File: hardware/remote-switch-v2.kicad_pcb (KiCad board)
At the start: 2 copper layers, 40 x 25 mm, 27 parts, among them J1 Debug, P1 CON-SENSOR2, P2 BOOT, U1 XMC1302-32, U2 RFM69HW, U3 DRILL, U4 DRILL, U5 DRILL, U6 DRILL

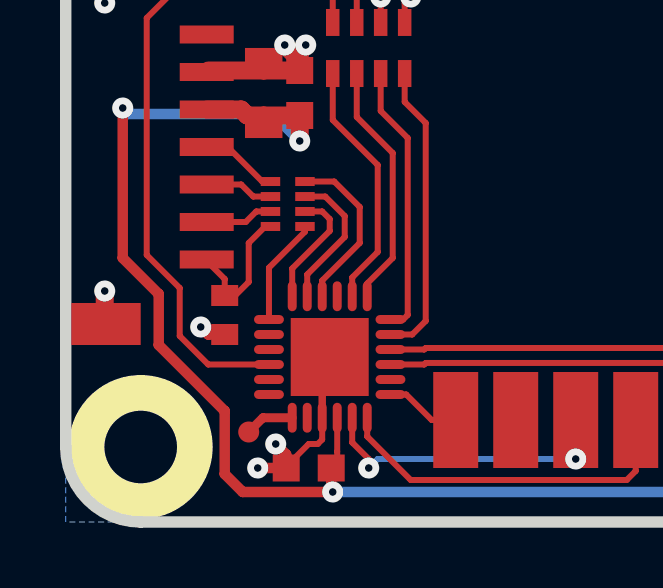
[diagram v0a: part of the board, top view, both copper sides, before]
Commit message: Change capacitor footprint(s) to C0402F
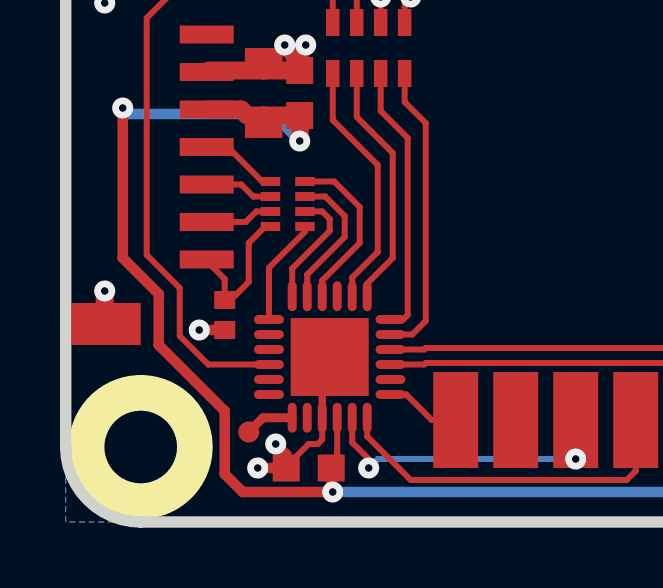
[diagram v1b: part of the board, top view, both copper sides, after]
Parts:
- C1: footprint C0402E -> kicad-libraries:C0402F
- C2: footprint C0805 -> kicad-libraries:C0805
- C3, C4, C5, C6: footprint C0603F -> kicad-libraries:C0603F
- P1: footprint CON-SENSOR2 -> kicad-libraries:CON-SENSOR2
- RP1: footprint 4X0402 -> kicad-libraries:4X0402
- RP2, RP3: footprint 4X0603 -> kicad-libraries:4X0603
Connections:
- P1 pad 1: (no net) -> Net-(P1-Pad1)
- RP3 pad 2: (no net) -> Net-(RP3-Pad2)
- RP3 pad 3: (no net) -> Net-(RP3-Pad3)
- RP3 pad 6: (no net) -> Net-(RP3-Pad6)
- RP3 pad 7: (no net) -> Net-(RP3-Pad7)
- U1 pad 14: (no net) -> Net-(U1-Pad14)
- U1 pad 2: (no net) -> Net-(U1-Pad2)
- U1 pad 21: (no net) -> Net-(U1-Pad21)
- U1 pad 3: (no net) -> Net-(U1-Pad3)
- U1 pad 5: (no net) -> Net-(U1-Pad5)
- U1 pad 6: (no net) -> Net-(U1-Pad6)
- U1 pad 8: (no net) -> Net-(U1-Pad8)
- U2 pad 1: (no net) -> Net-(U2-Pad1)
- U2 pad 10: (no net) -> Net-(U2-Pad10)
- U2 pad 13: (no net) -> Net-(U2-Pad13)
- U2 pad 14: (no net) -> Net-(U2-Pad14)
- U2 pad 15: (no net) -> Net-(U2-Pad15)

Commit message: Data Cleanup
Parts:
- moved U6 119.5 mm to (155.5, 78.8), turned to -90 degrees
- moved Fiducial_Mark 116.6 mm to (155.0, 83.3), turned to -90 degrees
- moved P2 113.8 mm to (152.5, 82.2), turned to 90 degrees
- moved G*** 112.6 mm to (156.8, 110.4), turned to 180 degrees
- moved U3 110.8 mm to (155.5, 113.8), turned to -90 degrees
- moved P1 108.0 mm to (145.5, 76.4), turned to 180 degrees
- moved RP2 106.9 mm to (148.8, 86.4), turned to -90 degrees
- moved C2 106.6 mm to (147.3, 82.9), turned to 0 degrees
- moved C3 106.0 mm to (147.3, 84.1), turned to 0 degrees
- moved RP1 101.3 mm to (143.6, 83.7), turned to 180 degrees
- moved VAL 101.2 mm to (145.5, 89.3), turned to 90 degrees
- moved U2 99.2 mm to (145.9, 96.3), turned to 0 degrees
- moved G*** 98.7 mm to (145.5, 96.3), turned to 90 degrees
- moved C1 97.7 mm to (139.9, 81.6), turned to 180 degrees
- moved VAL 97.3 mm to (145.5, 102.3), turned to 90 degrees
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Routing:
- net GND: track 76.9 -> 72.4 mm, vias 42 -> 39
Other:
- board size 40 x 25 mm -> 25 x 40 mm
- net class Antenna removed
- net class Default removed
- board text added: "Copyright Tinkerforge GmbH 2023. This documentation describes Open Hardware and is licensed under the CERN OHL v. 1.1. You may redistribute and modify this documentation under the terms of the CERN OHL v.1.1. (http://ohwr.org/cernohl). This documentation is distributed WITHOUT ANY EXPRESS OR IMPLIED WARRANTY, INCLUDING OF MERCHANTABILITY, SATISFACTORY QUALITY AND FITNESS FOR A PARTICULAR PURPOSE.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"
- board text removed: "Copyright Tinkerforge GmbH 2013. This documentation describes Open Hardware and is licensed under the CERN OHL v. 1.1. You may redistribute and modify this documentation under the terms of the CERN OHL v.1.1. (http://ohwr.org/cernohl). This documentation is distributed WITHOUT ANY EXPRESS OR IMPLIED WARRANTY, INCLUDING OF MERCHANTABILITY, SATISFACTORY QUALITY AND FITNESS FOR A PARTICULAR PURPOSE.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"
